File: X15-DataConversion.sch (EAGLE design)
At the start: 12 parts

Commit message: schematic actually finished now
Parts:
- added C6: 0.1uF, SparkFun-RF:0.1UF-0603-25V-5%
- added CAN_TRANCEIVER: MAX3058ASA+, CAN Tranceiver:MAX3058ASA+
- added CONNECTOR1: 3V3 -SWCLK-GND-SWDIO- NRST, CONN, Serial Wire Programming Headers:SWD_CONN
- added D3: Orange, SparkFun-LED:LED0603
- added R5: 82, SparkFun-Resistors:RESISTOR0603
- added R6, R7: 120, SparkFun-Resistors:RESISTOR0603
- added STM: STM32F042K6T6, IC, STM32F042K6T6:STM32F042K6T6
- U$1: value STM32F042K6T6 -> DATACONV->BACKPLANE; device X15 Data Conversion:STM32F042K6T6 -> CONN, DataConversion-Backplane Connector- SAMTEC CLT-107-01-T-D:DATACONV->BACKPLANE
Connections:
- new net CAN_H: CAN_TRANCEIVER.CANH, R6.2, R7.2, U$1.10
- new net CAN_L: CAN_TRANCEIVER.CANL, R6.1, R7.1, U$1.11
- new net N$1: D3.A, R5.1
- net 3.3V: now also C6.1, CAN_TRANCEIVER.VCC, CONNECTOR1.3V3, R5.2, STM.VDD, STM.VDDA, STM.VDDIO2, U$1.1; no longer U$1.VDD, U$1.VDDA, U$1.VDDIO2
- net ALERT1: now also STM.PB4, U$1.14; no longer U$1.PB4
- net ALERT2: now also STM.PB3, U$1.12; no longer U$1.PB3
- net C2_1: now also U$1.9
- net C2_2: now also U$1.7
- net CAN_RX: now also CAN_TRANCEIVER.RXD, STM.PA11; no longer U$1.PA11
- net CAN_TX: now also CAN_TRANCEIVER.TXD, STM.PA12; no longer U$1.PA12
- net CLK: now also STM.PA9, U$1.5; no longer U$1.PA9
- net DATA: now also STM.PA10, U$1.4; no longer U$1.PA10
- net GND: now also C6.2, CAN_TRANCEIVER.GND, CAN_TRANCEIVER.RS, CAN_TRANCEIVER.SHDN, CONNECTOR1.GND, D3.C, STM.PB8-BOOT0, STM.VSS, STM.VSS_2, U$1.2, U$1.3; no longer U$1.PB8-BOOT0, U$1.VSS, U$1.VSS_2
- net LED: now also STM.PA15; no longer U$1.PA15
- net N$6: now also STM.PB1; no longer U$1.PB1
- net N$7: now also STM.PB0; no longer U$1.PB0
- net NRST: now also CONNECTOR1.NRST, STM.NRST, U$1.13; no longer U$1.NRST
- net SWCLK: now also CONNECTOR1.SWCLK, STM.PA14, U$1.8; no longer U$1.PA14
- net SWDIO: now also CONNECTOR1.SWDIO, STM.PA13, U$1.6; no longer U$1.PA13
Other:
- note added: "CAN"
- note added: "Connectors"
- note added: "Power Indication LED"
- moved on the sheet: C1, C2, C3, C4, C5, D1, R1, R2, R3, R4, S1

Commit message: added oscillator
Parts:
- added C7, C8: 18pF, SparkFun-RF:0.1UF-0603-25V-5%
- added R9: 1.5k, SparkFun-Resistors:RESISTOR0603
- added Y1: ECS-80-18-30-JGN-TR, ECS-80-18-30-JGN-TR:ECS-80-18-30-JGN-TR
- CAN_TRANCEIVER: device CAN Tranceiver:MAX3058ASA+ -> IC,MAX3058ASA+:MAX3058ASA+
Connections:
- new net N$3: C8.1, R9.1, Y1.OUT/IN
- new net OSC_IN: C7.1, STM.PF0-OSC_IN, Y1.IN/OUT
- new net OSC_OUT: R9.2, STM.PF1-OSC_OUT
- net GND: now also C7.2, C8.2
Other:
- note added: "Oscillator"
- note added: "RS to ground for high-speed mode (1Mbps with shielded twisted-pair cable) RS to resistor to ground for slope-control mode (resistor value affects slew rates)"

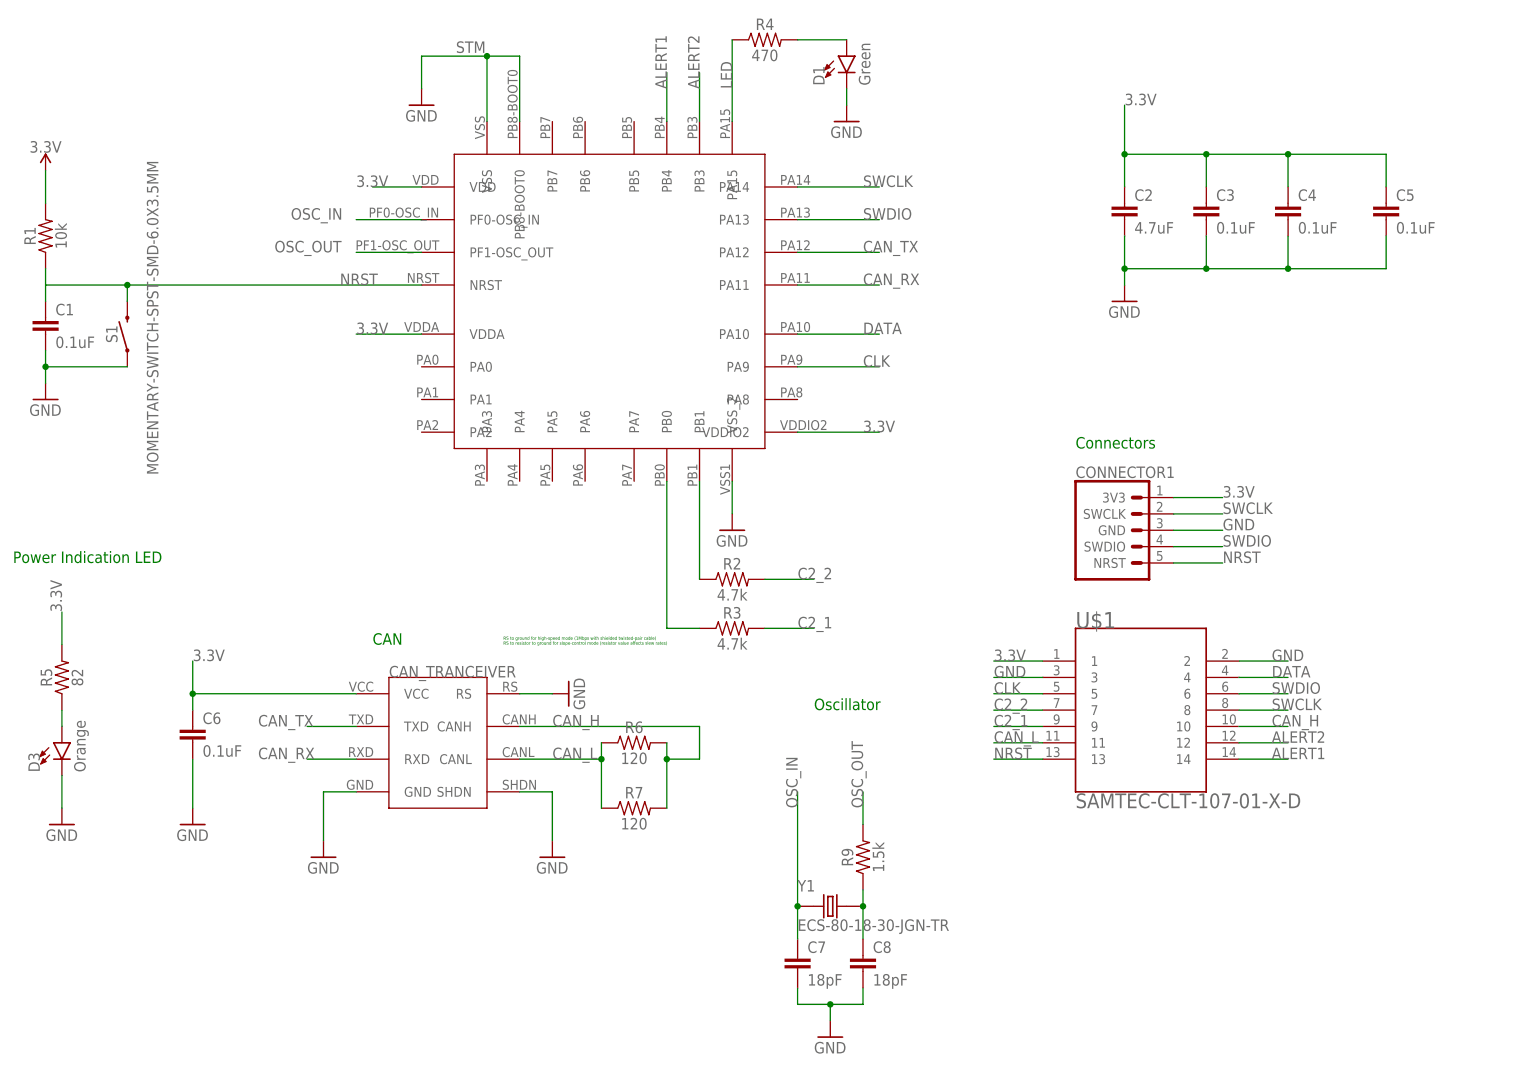
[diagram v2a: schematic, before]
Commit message: oscillator resistor and capacitor labels
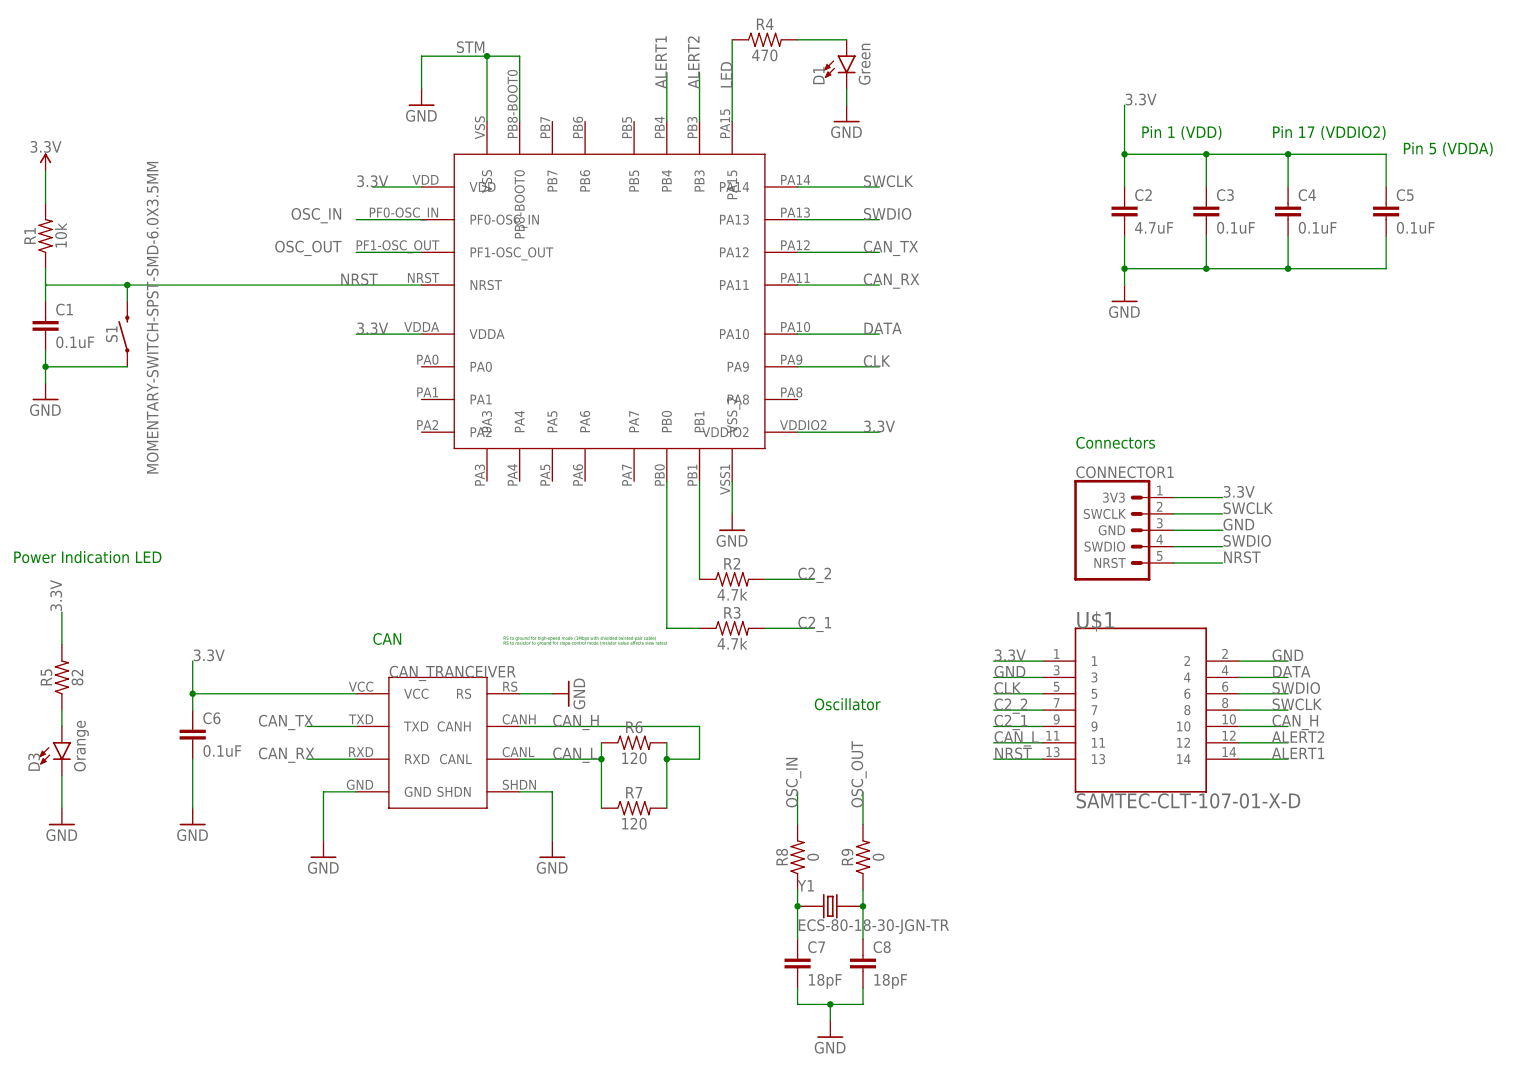
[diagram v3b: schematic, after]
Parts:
- added R8: 0, SparkFun-Resistors:RESISTOR0603
- R9: value 1.5k -> 0
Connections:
- net OSC_IN: now also R8.1, R8.2
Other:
- note added: "Pin 1 (VDD)"
- note added: "Pin 17 (VDDIO2)"
- note added: "Pin 5 (VDDA)"

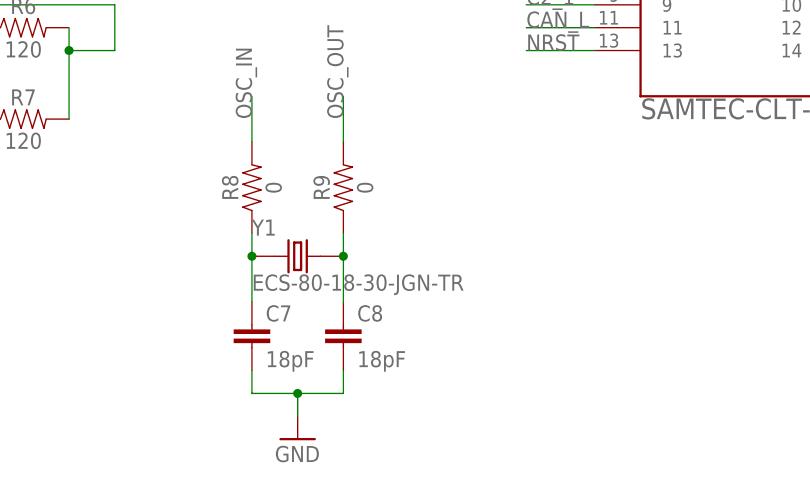
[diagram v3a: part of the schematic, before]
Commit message: replaced oscillator with same one as on Pi Shield
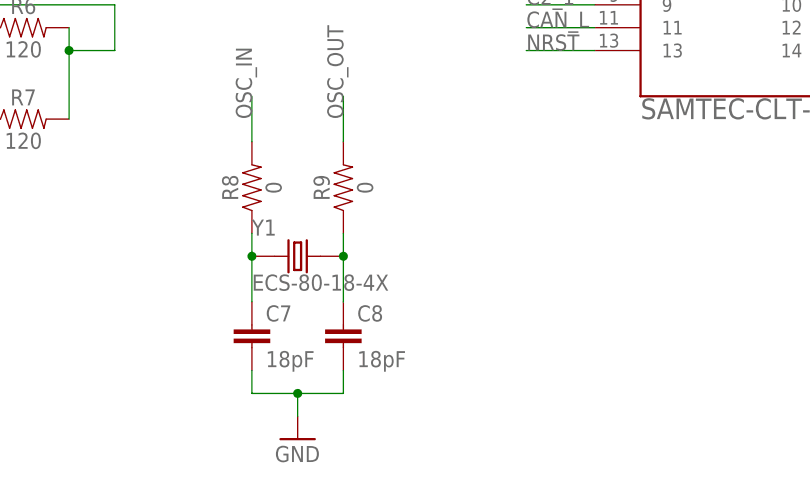
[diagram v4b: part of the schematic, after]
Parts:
- Y1: value ECS-80-18-30-JGN-TR -> ECS-80-18-4X; device ECS-80-18-30-JGN-TR:ECS-80-18-30-JGN-TR -> ECS-80-18-4X:ECS-80-18-4X
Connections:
- net N$3: now also Y1.2; no longer Y1.OUT/IN
- net OSC_IN: now also Y1.1; no longer Y1.IN/OUT
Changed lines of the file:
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@@
 <part name="C8" library="SparkFun-RF" deviceset="0.1UF" device="-0603-25V-5%" value="18pF"/>
 <part name="GND11" library="supply1" library_urn="urn:adsk.eagle:library:371" deviceset="GND" device=""/>
-<part name="Y1" library="ECS-80-18-30-JGN-TR" deviceset="ECS-80-18-30-JGN-TR" device=""/>
+<part name="Y1" library="ECS-80-18-4X" deviceset="ECS-80-18-4X" device=""/>
 <part name="R8" library="SparkFun-Resistors" deviceset="RESISTOR" device="0603" value="0"/>
 </parts>
@@
 <wire x1="137.16" y1="27.94" x2="137.16" y2="33.02" width="0.1524" layer="91"/>
 <pinref part="C7" gate="G$1" pin="1"/>
-<pinref part="Y1" gate="G$1" pin="IN/OUT"/>
+<pinref part="Y1" gate="G$1" pin="1"/>
 <pinref part="R8" gate="G$1" pin="1"/>
 <wire x1="137.16" y1="33.02" x2="137.16" y2="35.56" width="0.1524" layer="91"/>
@@
 <pinref part="R9" gate="G$1" pin="1"/>
 <wire x1="147.32" y1="27.94" x2="147.32" y2="33.02" width="0.1524" layer="91"/>
-<pinref part="Y1" gate="G$1" pin="OUT/IN"/>
+<pinref part="Y1" gate="G$1" pin="2"/>
 <wire x1="147.32" y1="33.02" x2="147.32" y2="35.56" width="0.1524" layer="91"/>
 <junction x="147.32" y="33.02"/>

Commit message: starting wiring
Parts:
- Y1: device ECS-80-18-4X:ECS-80-18-4X -> OTHER, ECS-80-18-4X:ECS-80-18-4X
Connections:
- removed net N$2: C1.1, R1.1
- new net N$3: C7.1, R8.1, Y1.1
- net NRST: now also C1.1, R1.1
- net OSC_IN: now also R9.2; no longer C7.1, R8.1, R8.2, Y1.1
- net OSC_OUT: now also R8.2; no longer R9.2
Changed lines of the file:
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@@
 <part name="D1" library="SparkFun-LED" deviceset="LED-GREEN" device="-0603-WE" value="Green"/>
 <part name="GND5" library="supply1" library_urn="urn:adsk.eagle:library:371" deviceset="GND" device=""/>
-<part name="SUPPLY1" library="SparkFun-PowerSymbols" deviceset="3.3V" device=""/>
 <part name="S1" library="SparkFun-Switches" deviceset="MOMENTARY-SWITCH-SPST" device="-SMD-6.0X3.5MM"/>
 <part name="GND4" library="supply1" library_urn="urn:adsk.eagle:library:371" deviceset="GND" device=""/>
@@
 <part name="C8" library="SparkFun-RF" deviceset="0.1UF" device="-0603-25V-5%" value="18pF"/>
 <part name="GND11" library="supply1" library_urn="urn:adsk.eagle:library:371" deviceset="GND" device=""/>
-<part name="Y1" library="ECS-80-18-4X" deviceset="ECS-80-18-4X" device=""/>
+<part name="Y1" library="OTHER, ECS-80-18-4X" deviceset="ECS-80-18-4X" device=""/>
 <part name="R8" library="SparkFun-Resistors" deviceset="RESISTOR" device="0603" value="0"/>
 </parts>
@@
 <attribute name="VALUE" x="142.24" y="152.4" size="1.778" layer="96"/>
 </instance>
-<instance part="SUPPLY1" gate="G$1" x="20.32" y="147.32" smashed="yes">
-<attribute name="VALUE" x="20.32" y="150.114" size="1.778" layer="96" font="vector" align="bottom-center"/>
-</instance>
 <instance part="S1" gate="G$1" x="33.02" y="121.92" smashed="yes" rot="R90">
 <attribute name="NAME" x="31.496" y="121.92" size="1.778" layer="95" font="vector" rot="R90" align="bottom-center"/>
@@
 </instance>
 <instance part="Y1" gate="G$1" x="142.24" y="33.02" smashed="yes">
-<attribute name="NAME" x="137.14743125" y="35.315540625" size="1.78543125" layer="95"/>
 <attribute name="VALUE" x="137.14506875" y="29.19645" size="1.78431875" layer="96"/>
 </instance>
@@
 </busses>
 <nets>
-<net name="N$2" class="0">
-<segment>
-<pinref part="R1" gate="G$1" pin="1"/>
-<pinref part="C1" gate="G$1" pin="1"/>
-<wire x1="20.32" y1="132.08" x2="20.32" y2="127" width="0.1524" layer="91"/>
-</segment>
-</net>
 <net name="GND" class="0">
 <segment>
@@
 <pinref part="STM" gate="G$1" pin="NRST"/>
 <wire x1="78.74" y1="129.54" x2="33.02" y2="129.54" width="0.1524" layer="91"/>
+<label x="66.04" y="129.54" size="1.778" layer="95"/>
+<pinref part="R1" gate="G$1" pin="1"/>
+<pinref part="C1" gate="G$1" pin="1"/>
+<wire x1="33.02" y1="129.54" x2="20.32" y2="129.54" width="0.1524" layer="91"/>
+<wire x1="20.32" y1="132.08" x2="20.32" y2="129.54" width="0.1524" layer="91"/>
+<wire x1="20.32" y1="129.54" x2="20.32" y2="127" width="0.1524" layer="91"/>
+<junction x="20.32" y="129.54"/>
 <pinref part="S1" gate="G$1" pin="2"/>
-<wire x1="33.02" y1="129.54" x2="20.32" y2="129.54" width="0.1524" layer="91"/>
 <wire x1="33.02" y1="127" x2="33.02" y2="129.54" width="0.1524" layer="91"/>
 <junction x="33.02" y="129.54"/>
-<label x="66.04" y="129.54" size="1.778" layer="95"/>
 </segment>
 <segment>
@@
 </net>
 <net name="3.3V" class="0">
-<segment>
-<pinref part="R1" gate="G$1" pin="2"/>
-<pinref part="SUPPLY1" gate="G$1" pin="3.3V"/>
-<wire x1="20.32" y1="142.24" x2="20.32" y2="147.32" width="0.1524" layer="91"/>
-</segment>
 <segment>
 <pinref part="STM" gate="G$1" pin="VDDA"/>
@@
 </segment>
 <segment>
-<pinref part="CAN_TRANCEIVER" gate="G$1" pin="VCC"/>
-<wire x1="68.58" y1="66.04" x2="43.18" y2="66.04" width="0.1524" layer="91"/>
-<wire x1="43.18" y1="66.04" x2="43.18" y2="71.12" width="0.1524" layer="91"/>
-<label x="43.18" y="71.12" size="1.778" layer="95"/>
 <pinref part="C6" gate="G$1" pin="1"/>
 <wire x1="43.18" y1="63.5" x2="43.18" y2="66.04" width="0.1524" layer="91"/>
+<label x="43.18" y="76.2" size="1.778" layer="95" rot="R90"/>
+<pinref part="CAN_TRANCEIVER" gate="G$1" pin="VCC"/>
+<wire x1="43.18" y1="66.04" x2="43.18" y2="76.2" width="0.1524" layer="91"/>
+<wire x1="68.58" y1="66.04" x2="43.18" y2="66.04" width="0.1524" layer="91"/>
 <junction x="43.18" y="66.04"/>
+</segment>
+<segment>
+<pinref part="R1" gate="G$1" pin="2"/>
+<wire x1="20.32" y1="142.24" x2="20.32" y2="147.32" width="0.1524" layer="91"/>
+<label x="20.32" y="147.32" size="1.778" layer="95" rot="R90"/>
 </segment>
 </net>
@@
 <pinref part="STM" gate="G$1" pin="PF0-OSC_IN"/>
 <wire x1="78.74" y1="139.7" x2="68.58" y2="139.7" width="0.1524" layer="91"/>
-<label x="58.42" y="139.7" size="1.778" layer="95"/>
-</segment>
-<segment>
-<wire x1="137.16" y1="27.94" x2="137.16" y2="33.02" width="0.1524" layer="91"/>
-<pinref part="C7" gate="G$1" pin="1"/>
+</segment>
+<segment>
+<pinref part="R9" gate="G$1" pin="2"/>
+<wire x1="147.32" y1="45.72" x2="147.32" y2="50.8" width="0.1524" layer="91"/>
+<label x="147.32" y="48.26" size="1.778" layer="95" rot="R90"/>
+</segment>
+</net>
+<net name="OSC_OUT" class="0">
+<segment>
+<pinref part="STM" gate="G$1" pin="PF1-OSC_OUT"/>
+<wire x1="78.74" y1="134.62" x2="68.58" y2="134.62" width="0.1524" layer="91"/>
+</segment>
+<segment>
+<pinref part="R8" gate="G$1" pin="2"/>
+<wire x1="137.16" y1="45.72" x2="137.16" y2="50.8" width="0.1524" layer="91"/>
+<label x="137.16" y="48.26" size="1.778" layer="95" rot="R90"/>
+</segment>
+</net>
+<net name="N$3" class="0">
+<segment>
 <pinref part="Y1" gate="G$1" pin="1"/>
 <pinref part="R8" gate="G$1" pin="1"/>
 <wire x1="137.16" y1="33.02" x2="137.16" y2="35.56" width="0.1524" layer="91"/>
+<pinref part="C7" gate="G$1" pin="1"/>
+<wire x1="137.16" y1="27.94" x2="137.16" y2="33.02" width="0.1524" layer="91"/>
 <junction x="137.16" y="33.02"/>
 </segment>
-<segment>
-<pinref part="R8" gate="G$1" pin="2"/>
-<wire x1="137.16" y1="45.72" x2="137.16" y2="50.8" width="0.1524" layer="91"/>
-<label x="137.16" y="48.26" size="1.778" layer="95" rot="R90"/>
-</segment>
-</net>
-<net name="OSC_OUT" class="0">
-<segment>
-<pinref part="STM" gate="G$1" pin="PF1-OSC_OUT"/>
-<wire x1="78.74" y1="134.62" x2="68.58" y2="134.62" width="0.1524" layer="91"/>
-<label x="55.88" y="134.62" size="1.778" layer="95"/>
-</segment>
-<segment>
-<pinref part="R9" gate="G$1" pin="2"/>
-<wire x1="147.32" y1="45.72" x2="147.32" y2="50.8" width="0.1524" layer="91"/>
-<label x="147.32" y="48.26" size="1.778" layer="95" rot="R90"/>
-</segment>
-</net>
-<net name="N$3" class="0">
-<segment>
+</net>
+<net name="N$4" class="0">
+<segment>
+<pinref part="Y1" gate="G$1" pin="2"/>
+<pinref part="R9" gate="G$1" pin="1"/>
+<wire x1="147.32" y1="33.02" x2="147.32" y2="35.56" width="0.1524" layer="91"/>
 <pinref part="C8" gate="G$1" pin="1"/>
-<pinref part="R9" gate="G$1" pin="1"/>
 <wire x1="147.32" y1="27.94" x2="147.32" y2="33.02" width="0.1524" layer="91"/>
-<pinref part="Y1" gate="G$1" pin="2"/>
-<wire x1="147.32" y1="33.02" x2="147.32" y2="35.56" width="0.1524" layer="91"/>
 <junction x="147.32" y="33.02"/>
 </segment>
